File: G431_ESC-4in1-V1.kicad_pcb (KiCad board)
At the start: 4 copper layers, 46 x 55.8 mm, 223 parts, among them J1 Conn_01x02, J10 Conn_01x03, J11 Conn_01x03, J2 Conn_01x10, J3 Conn_01x04, J4 Conn_01x04, J5 Conn_01x04, J6 Conn_01x03, J7 Conn_01x04, J8 Conn_01x03, J9 Conn_01x10, Q1 TPH1R204PB, Q10 TPH1R204PB, Q11 TPH1R204PB, Q12 TPH1R204PB, Q13 TPH1R204PB, Q14 TPH1R204PB, Q15 TPH1R204PB, Q16 TPH1R204PB, Q17 TPH1R204PB, Q18 TPH1R204PB, Q19 TPH1R204PB, Q2 TPH1R204PB, Q20 TPH1R204PB, Q21 TPH1R204PB, Q22 TPH1R204PB, Q23 TPH1R204PB, Q24 TPH1R204PB, Q3 TPH1R204PB, Q4 TPH1R204PB, Q5 TPH1R204PB, Q6 TPH1R204PB, Q7 TPH1R204PB, Q8 TPH1R204PB, Q9 TPH1R204PB, U1 FD6288Q, U10 FD6288Q, U11 FD6288Q, U12 STM32G431KBU6, U13 L78L12_SOT89, U14 MP4560_QFN10, U15 DTOM, U2 STM32G431KBU6, U3 L78L12_SOT89, U4 LP2985-3.3, U5 INA139, U6 STM32G431KBU6, U7 OPA340NA, U8 FD6288Q, U9 STM32G431KBU6

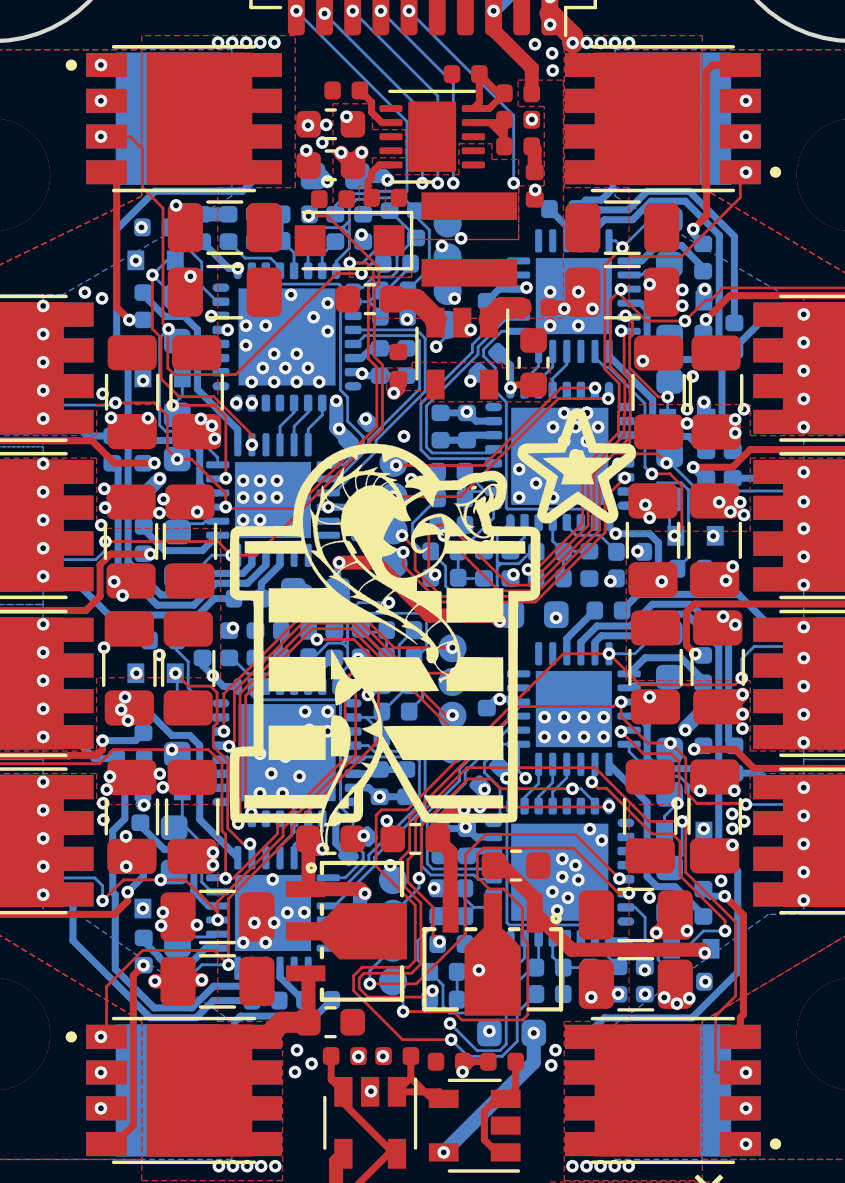
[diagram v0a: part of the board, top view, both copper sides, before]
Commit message: Got rid of trace on GND plane and moved some small stuff around
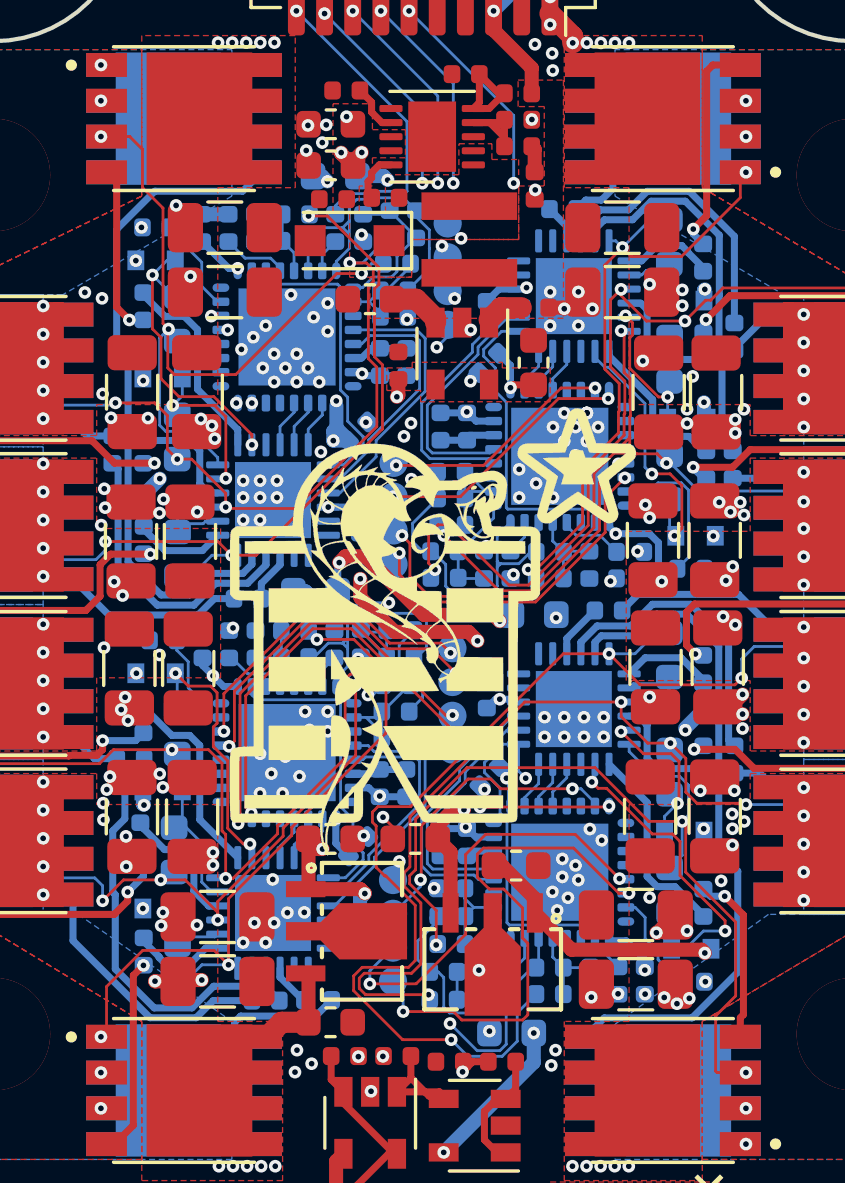
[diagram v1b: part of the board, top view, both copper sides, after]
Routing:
- net VCC_Shunt: track 15.7 -> 21.2 mm, vias 134 -> 136
- net +3V3: track 93.8 -> 95.0 mm
- net /MCU_4/SWDIO: track 9.37 -> 9.95 mm
- net /Curent Sense/CURR: track 47.3 -> 47.8 mm
- net /PWM_1: track 48.0 -> 48.5 mm
- net GND: track 6.05 -> 6.23 mm, vias 205 -> 206
- added copper zone on In2.Cu, net +3V3
